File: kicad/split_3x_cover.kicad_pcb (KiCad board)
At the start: 2 copper layers, 30.5 x 65 mm, 3 parts

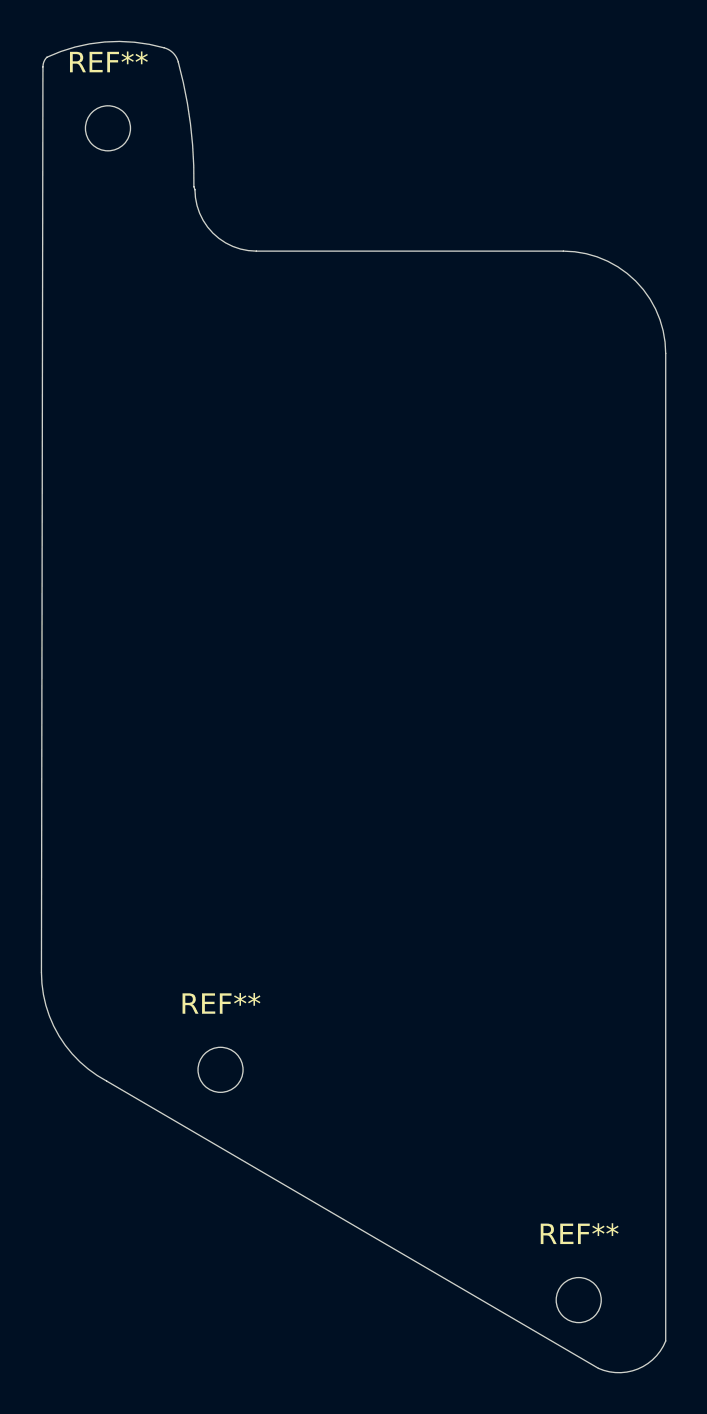
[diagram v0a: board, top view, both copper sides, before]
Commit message: added millmax hotswappable sockets
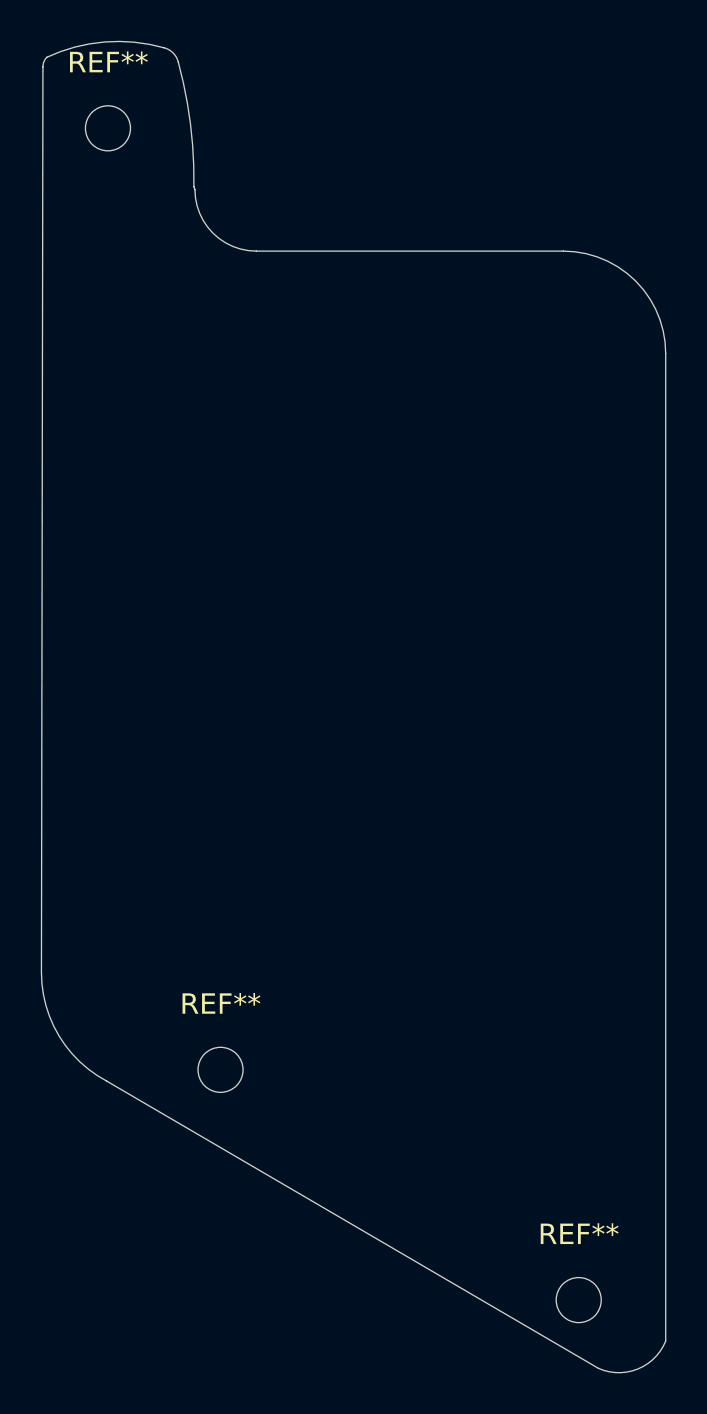
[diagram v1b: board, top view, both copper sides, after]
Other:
- net class Default removed
- net class Power removed
- net class TRRSData removed
